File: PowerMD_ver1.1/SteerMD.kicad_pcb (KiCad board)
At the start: 2 copper layers, 75 x 88 mm, 232 parts, among them P1 SWD, P10 OUT_1, P11 ENC_0, P13 ENC_1, P14 I/O_1, P15 OUT_0, P2 MOTOR_COOLING, P3 CAN, P4 CAN, P5 SERIAL, P6 I/O_0, P7 FAN, P8 BATT_IN, P9 BATT_IN, Q1 MOSFET_N, Q2 MOSFET_N, Q3 MOSFET_N, Q4 MOSFET_N, Q5 MOSFET_N, Q6 MOSFET_N, Q7 MOSFET_N, Q8 MOSFET_N, SW1 RST, SW3 SW0, SW4 SW1, U1 MAX3051, U10 ACS758, U11 POWER_ON, U12 SI8274, U13 ACS758, U14 SI8274, U15 AZ1086H, U16 LOGO, U17 AQM0802, U18 LTC2644, U19 ADRESS, U2 BD9G101, U3 STM32F405RG, U4 SI8274, U5 SI8900, U6 ADC_~RST, U7 MCP16331, U8 SI8274, U9 BD33FA1, Y1 8MHz

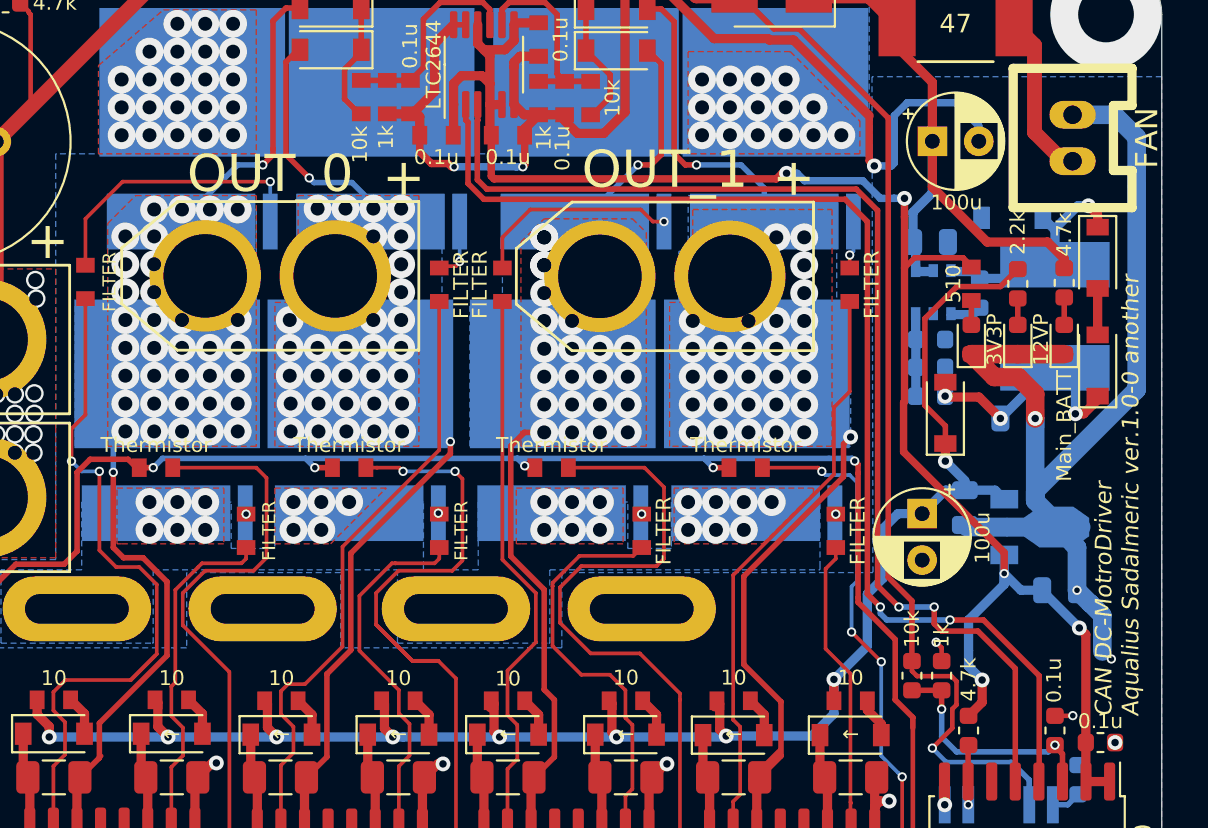
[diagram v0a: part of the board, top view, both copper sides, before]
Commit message: ビアの開け方(この前ちらっとネット上で観測した開け方参考)により，放熱性能が上がるかチェックするMD作成
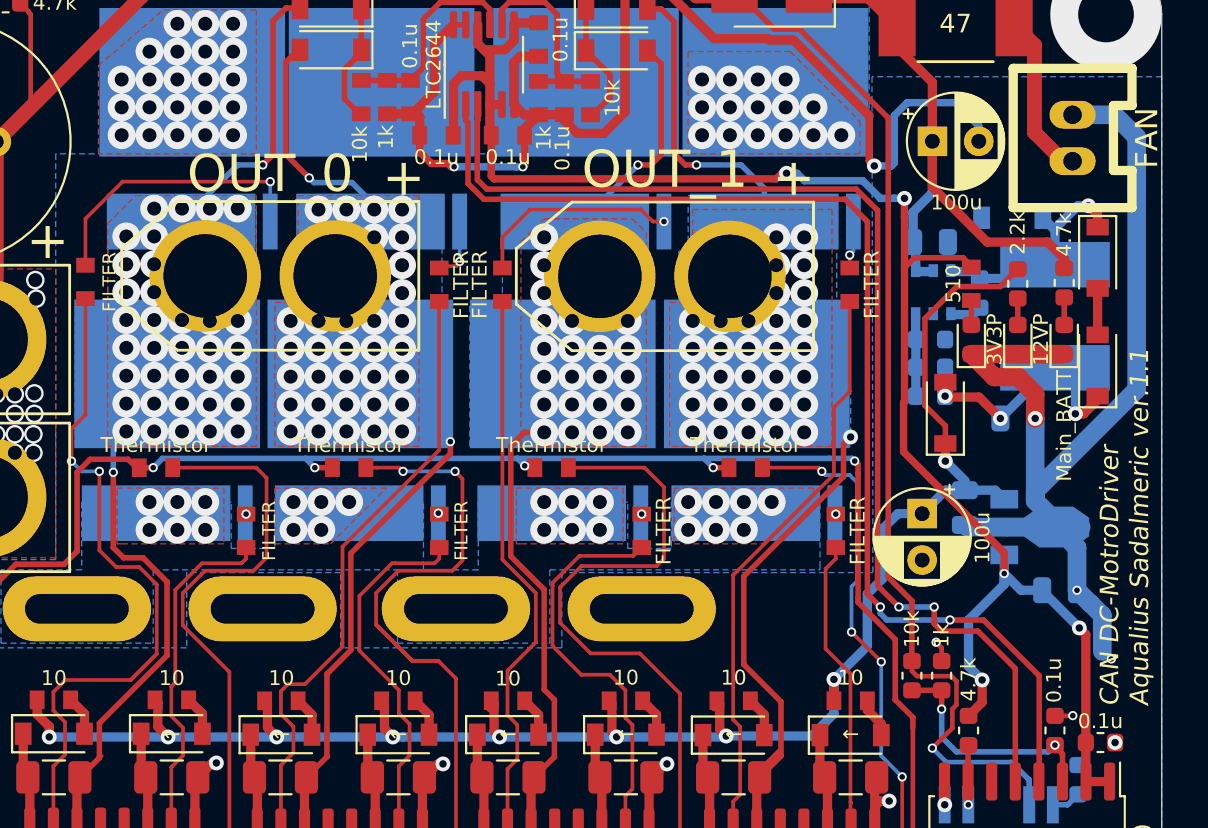
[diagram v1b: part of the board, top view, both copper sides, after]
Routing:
- net /OUT1_R: vias 30 -> 33
- net /OUT1_L: vias 24 -> 23
- net /OUT0_R: vias 33 -> 35
- net /OUT0_L: vias 36 -> 37
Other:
- board text added: "CAN DC-MotroDriver Aqualius Sadalmeric ver.1.1"
- board text removed: "CAN DC-MotroDriver Aqualius Sadalmeric ver.1.0-0 another"
